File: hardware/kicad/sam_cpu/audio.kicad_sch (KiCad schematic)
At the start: 45 parts, among them J10 J10 SPEAKERS, U22 PCM5102A, U23 TDA2030A, U24 TDA2030A

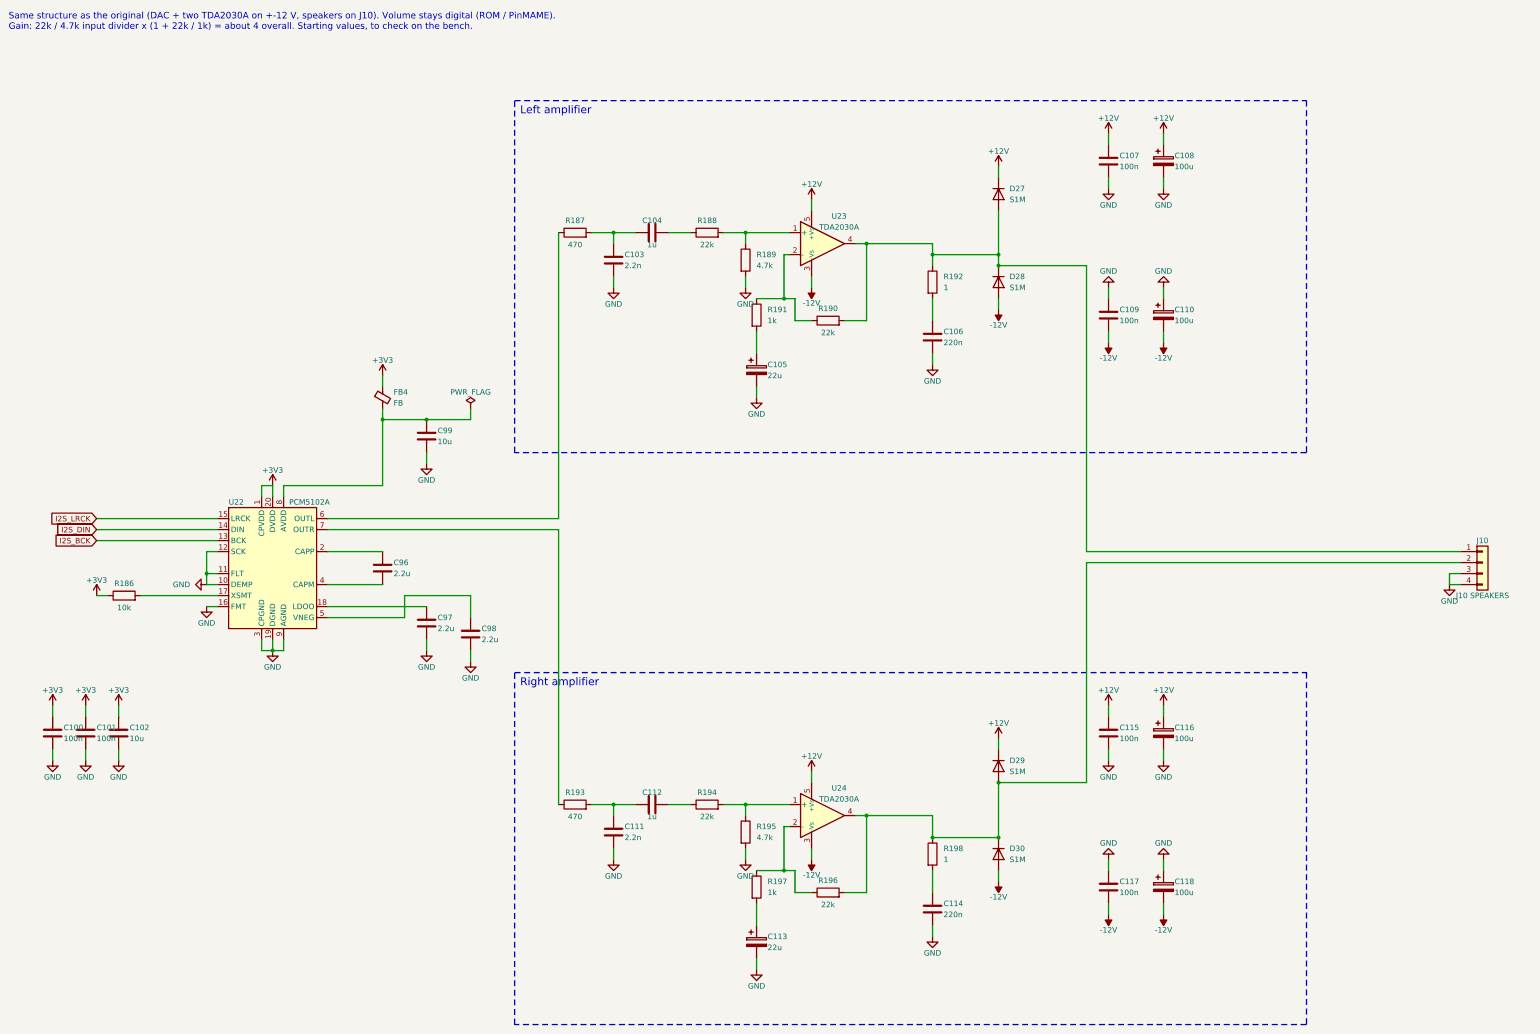
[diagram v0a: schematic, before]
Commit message: Add RTC, test points and stereo speaker connector; place all parts on 2 layers
Schematic: DS3231MZ real-time clock on the Pi I2C1 with a CR2032 holder,
22 test points (rails, bus, strobes, switch chain, VREF, DAC outputs) and
J22, a second KK-396 speaker connector with L and R as separate pairs.
ERC 0 errors, generated netlist matches the intended nets.

PCB: 2 copper layers. The RP2354B sits near J9 with its USB-C on the top
edge 13 mm from the USB pins; decoupling, regulator and crystal parts on
their pins; every other part grouped by sheet next to its connector, low
parts only under the Pi. J17 and J22 on the right edge; Pi and J5 12 mm
lower to fit the audio parts.

Co-Authored-By: Claude Opus 5.5 (1M context) <noreply@anthropic.com>
Claude-Session: https://claude.ai/code/session_01ExuDVoDDDHhVWjb8EwVzYb
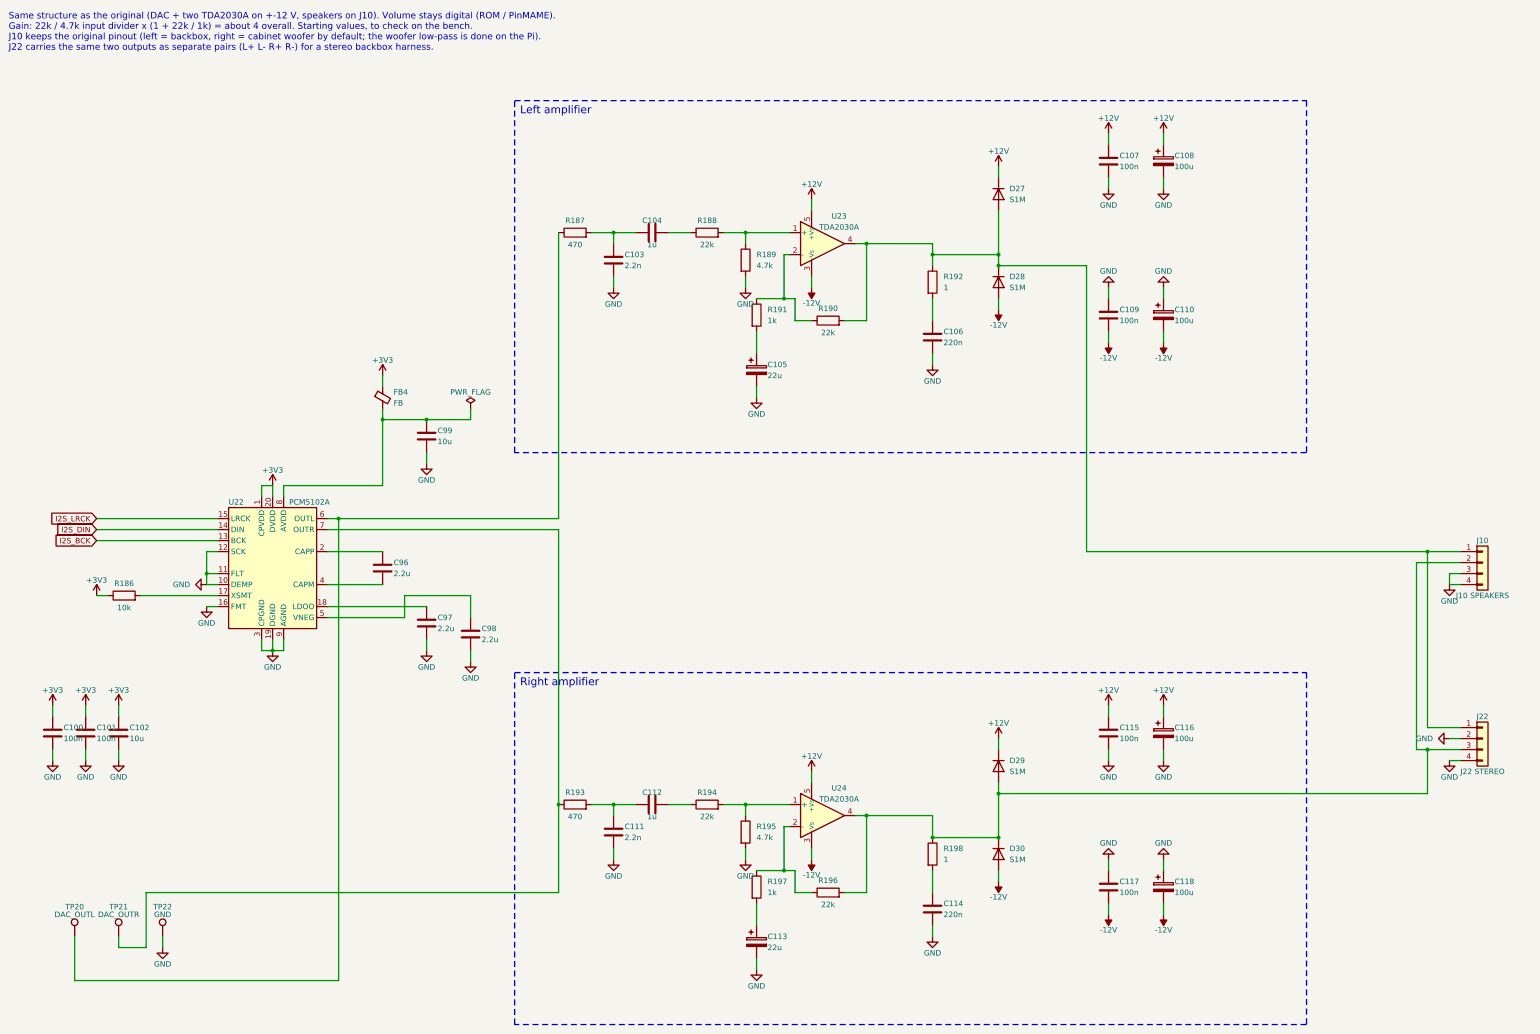
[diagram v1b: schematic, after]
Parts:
- added J22: J22 STEREO, Connector_Molex:Molex_KK-396_A-41791-0004_1x04_P3.96mm_Vertical, symbol Connector_Generic:Conn_01x04
- added TP20: DAC_OUTL, TestPoint:TestPoint_Pad_D1.5mm, symbol Connector:TestPoint
- added TP21: DAC_OUTR, TestPoint:TestPoint_Pad_D1.5mm, symbol Connector:TestPoint
- added TP22: GND, TestPoint:TestPoint_Pad_D1.5mm, symbol Connector:TestPoint
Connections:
- net GND: now also J22.2 (Pin_2), J22.4 (Pin_4), TP22.1
- net at R187.1, U22.6 (OUTL): now also TP20.1
- net at R193.1, U22.7 (OUTR): now also TP21.1
- net at D29.2 (A), D30.1 (K), J10.2 (Pin_2)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: now also J22.3 (Pin_3)
- net at D27.2 (A), D28.1 (K), J10.1 (Pin_1)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: now also J22.1 (Pin_1)
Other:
- note added: "Same structure as the original (DAC + two TDA2030A on +-12 V, speakers on J10). Volume stays digital (ROM / PinMAME). Gain: 22k / 4.7k input divider x (1 + 22k / 1k) = about 4 overall. Starting values, to check on the bench. J10 keeps the original pinout (left = backbox, right = cabinet woofer by default; the woofer low-pass is done on the Pi). J22 carries the same two outputs as separate pairs (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"
- note removed: "Same structure as the original (DAC + two TDA2030A on +-12 V, speakers on J10). Volume stays digital (ROM / PinMAME). Gain: 22k / 4.7k input divider x (1 + 22k / 1k) = about 4 overall. Starting values, to check on the bench."

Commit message: Audio on external 12 V with TDA7297 stereo + subwoofer amps, NCP1117, guide regulator layout
- Remove the +-12 V input from J11; J23 external +12 V with polyfuse and TVS
- Replace the two TDA2030A with a TDA7297 bridge amp for left/right (J10, J22)
  and a second TDA7297 for the subwoofer (J24), fed by an (L+R)/2 110 Hz
  Sallen-Key low-pass (OPA1678); shared standby and RP2354B-controlled mute
- AMS1117 -> NCP1117-3.3 (ceramic-stable, as in the RP2350 guide), 10 uF 1206
- L1 and crystal part numbers from the RP2350 hardware guide
- Place the core regulator parts by hand following the Pico 2 layout; amps in a
  row with a heatsink keep-out; J23/J22/J24 on the right edge

Co-Authored-By: Claude Opus 5.5 (1M context) <noreply@anthropic.com>
Claude-Session: https://claude.ai/code/session_01ExuDVoDDDHhVWjb8EwVzYb
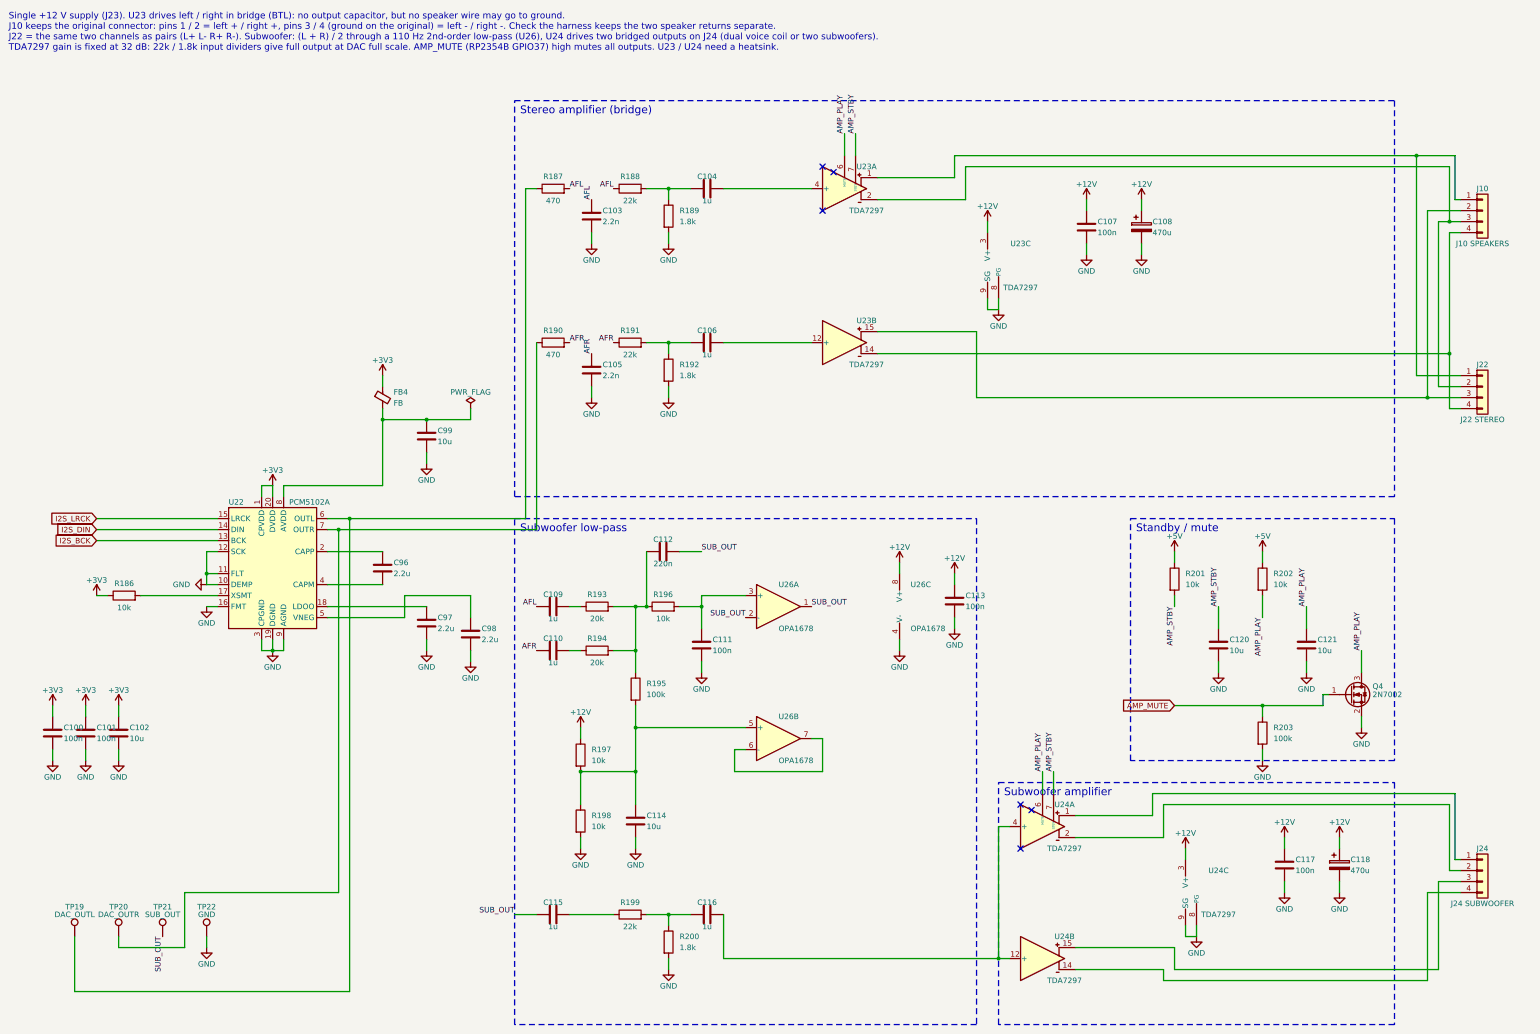
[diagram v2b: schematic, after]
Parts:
- removed D27, D28, D29, D30: S1M, Diode_SMD:D_SMA, symbol Device:D
- added C120, C121: 10u, Capacitor_SMD:C_0805_2012Metric, symbol Device:C
- added J24: J24 SUBWOOFER, Connector_Molex:Molex_KK-396_A-41791-0004_1x04_P3.96mm_Vertical, symbol Connector_Generic:Conn_01x04
- added Q4: 2N7002, Package_TO_SOT_SMD:SOT-23, symbol Transistor_FET:2N7002
- added R199: 22k, Resistor_SMD:R_0603_1608Metric, symbol Device:R
- added R200: 1.8k, Resistor_SMD:R_0603_1608Metric, symbol Device:R
- added R201, R202: 10k, Resistor_SMD:R_0603_1608Metric, symbol Device:R
- added R203: 100k, Resistor_SMD:R_0603_1608Metric, symbol Device:R
- added TP19: DAC_OUTL, TestPoint:TestPoint_Pad_D1.5mm, symbol Connector:TestPoint
- added unit 3 of U23
- added unit 2 of U23
- added unit 3 of U24
- added unit 2 of U24
- added U26: OPA1678, Package_SO:SOIC-8_3.9x4.9mm_P1.27mm, symbol Amplifier_Operational:OPA1678
- C105: value 22u -> 2.2n; footprint Capacitor_SMD:CP_Elec_6.3x7.7 -> Capacitor_SMD:C_0603_1608Metric; symbol Device:C_Polarized -> Device:C
- C106: value 220n -> 1u
- C108, C118: value 100u -> 470u
- C109, C115: value 100n -> 1u
- C110, C116: value 100u -> 1u; footprint Capacitor_SMD:CP_Elec_6.3x7.7 -> Capacitor_SMD:C_0603_1608Metric; symbol Device:C_Polarized -> Device:C
- C111: value 2.2n -> 100n
- C112: value 1u -> 220n
- C113: value 22u -> 100n; footprint Capacitor_SMD:CP_Elec_6.3x7.7 -> Capacitor_SMD:C_0603_1608Metric; symbol Device:C_Polarized -> Device:C
- C114: value 220n -> 10u; footprint Capacitor_SMD:C_0603_1608Metric -> Capacitor_SMD:C_0805_2012Metric
- R189: value 4.7k -> 1.8k
- R190: value 22k -> 470
- R191: value 1k -> 22k
- R192: value 1 -> 1.8k; footprint Resistor_SMD:R_1206_3216Metric -> Resistor_SMD:R_0603_1608Metric
- R193: value 470 -> 20k
- R194: value 22k -> 20k
- R195: value 4.7k -> 100k
- R196: value 22k -> 10k
- R197: value 1k -> 10k
- R198: value 1 -> 10k; footprint Resistor_SMD:R_1206_3216Metric -> Resistor_SMD:R_0603_1608Metric
- TP20: value DAC_OUTL -> DAC_OUTR
- TP21: value DAC_OUTR -> SUB_OUT
- U23, U24: value TDA2030A -> TDA7297; footprint Package_TO_SOT_THT:TO-220-5_P3.4x3.7mm_StaggerOdd_Lead3.8mm_Vertical -> Package_TO_SOT_THT:TO-220-15_P2.54x5.08mm_StaggerOdd_Lead4.58mm_Vertical; symbol Amplifier_Audio:TDA2030 -> Amplifier_Audio:TDA7297
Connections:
- net +12V: now also C113.1, C117.1, C118.1, R197.1, U23.13 (V+), U23.3 (V+), U24.13 (V+), U24.3 (V+), U26.8 (V+); no longer C115.1, C116.1, U23.5 (+Vs), U24.5 (+Vs)
- net GND: now also C117.2, C118.2, R192.2, R198.2, C120.2, C121.2, Q4.2 (S), R200.2, R203.2, U23.8 (PG), U23.9 (SG), U24.8 (PG), U24.9 (SG), U26.4 (V-); no longer C106.2, C109.1, C110.1, C115.2, C116.2, C117.1, C118.1, J10.3 (Pin_3), J10.4 (Pin_4), J22.2 (Pin_2), J22.4 (Pin_4), R195.2
- net at R187.1, U22.6 (OUTL): now also TP19.1; no longer TP20.1
- net at R191.2: now also C106.1, R192.1; no longer C105.1
- net at C112.1, R193.2: now also R194.2, R195.1, R196.1; no longer C111.1
- net at C114.1: now also R195.2, R197.2, R198.1, U26.5 (+); no longer R198.2
- net at C104.2: now also U23.4 (+); no longer R188.1
- net at R188.2, R189.1: now also C104.1; no longer U23.1 (+)
- net AFL: now reaches C103.1, R187.2
- net AFL: now also C109.1, R188.1; no longer C104.1
- net at R194.1: now also C110.2; no longer C112.2
- removed net -12V: C109.2, C110.2, C117.2, C118.2, U23.3 (-Vs), U24.3 (-Vs)
- new net: R190.1, TP20.1, U22.7 (OUTR)
- new net: C109.2, R193.1
- new net: J10.1 (Pin_1), J22.1 (Pin_1), U23.1
- new net: J10.3 (Pin_3), J22.2 (Pin_2), U23.2
- new net: J10.2 (Pin_2), J22.3 (Pin_3), U23.15
- new net: J10.4 (Pin_4), J22.4 (Pin_4), U23.14
- new net: C116.1, R199.2, R200.1
- new net: C116.2, U24.12 (+), U24.4 (+)
- new net: C111.1, R196.2, U26.3 (+)
- new net: C115.2, R199.1
- new net: C106.2, U23.12 (+)
- new net: J24.4 (Pin_4), U24.14
- new net: J24.3 (Pin_3), U24.15
- new net: J24.1 (Pin_1), U24.1
- new net: J24.2 (Pin_2), U24.2
- new net: U26.6 (-), U26.7
- new net +5V: R201.1, R202.1
- new net AFR: C105.1, C110.1, R190.2, R191.1
- new net AMP_MUTE: Q4.1 (G), R203.1
- new net AMP_PLAY: C121.1, Q4.3 (D), R202.2, U23.6 (MUTE), U24.6 (MUTE)
- new net AMP_STBY: C120.1, R201.2, U23.7 (STBY), U24.7 (STBY)
- new net SUB_OUT: C112.2, C115.1, TP21.1, U26.1, U26.2 (-)
- no-connect marks 0 -> 6
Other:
- note added: "Single +12 V supply (J23). U23 drives left / right in bridge (BTL): no output capacitor, but no speaker wire may go to ground. J10 keeps the original connector: pins 1 / 2 = left + / right +, pins 3 / 4 (ground on the original) = left - / right -. Check the harness keeps the two speaker returns separate. J22 = the same two channels as pairs (L+ L- R+ R-). Subwoofer: (L + R) / 2 through a 110 Hz 2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"
- note added: "Standby / mute"
- note added: "Stereo amplifier (bridge)"
- note added: "Subwoofer amplifier"
- note added: "Subwoofer low-pass"
- note removed: "Left amplifier"
- note removed: "Right amplifier"
- note removed: "Same structure as the original (DAC + two TDA2030A on +-12 V, speakers on J10). Volume stays digital (ROM / PinMAME). Gain: 22k / 4.7k input divider x (1 + 22k / 1k) = about 4 overall. Starting values, to check on the bench. J10 keeps the original pinout (left = backbox, right = cabinet woofer by default; the woofer low-pass is done on the Pi). J22 carries the same two outputs as separate pairs (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"
- title: Audio: Pi I2S -> PCM5102A -> 2 x TDA2030A on +-12 V -> J10 -> Audio: PCM5102A, TDA7297 stereo + subwoofer (+12 V)
- moved on the sheet: C103, C104, C106, C107, C108, C109, C111, C112, C114, C115, C117, C118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
